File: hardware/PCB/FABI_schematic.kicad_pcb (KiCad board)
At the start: 2 copper layers, 78 x 55 mm, 27 parts, among them J1 Cliff_68125, J10 Conn_01x03_Male, J2 Cliff_68125, J3 Cliff_68125, J4 Cliff_68125, J5 Cliff_68125, J6 Cliff_68125, J7 Cliff_68125, J8 Cliff_68125, J9 Conn_02x05_Odd_Even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

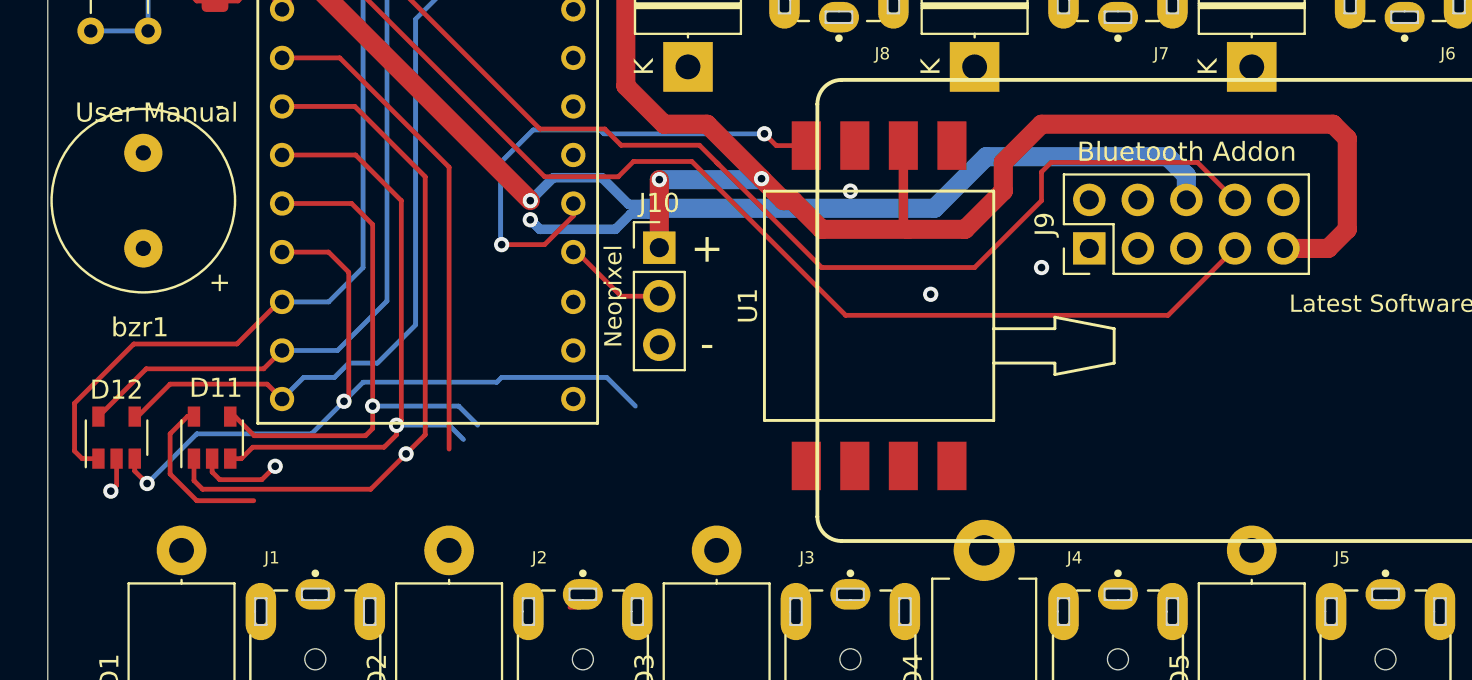
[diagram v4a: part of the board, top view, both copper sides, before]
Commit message: +Display header & 3D design of display to find position Signed-off-by: fussthalerandreas <fussthaler.andreas1997@gmail.com>
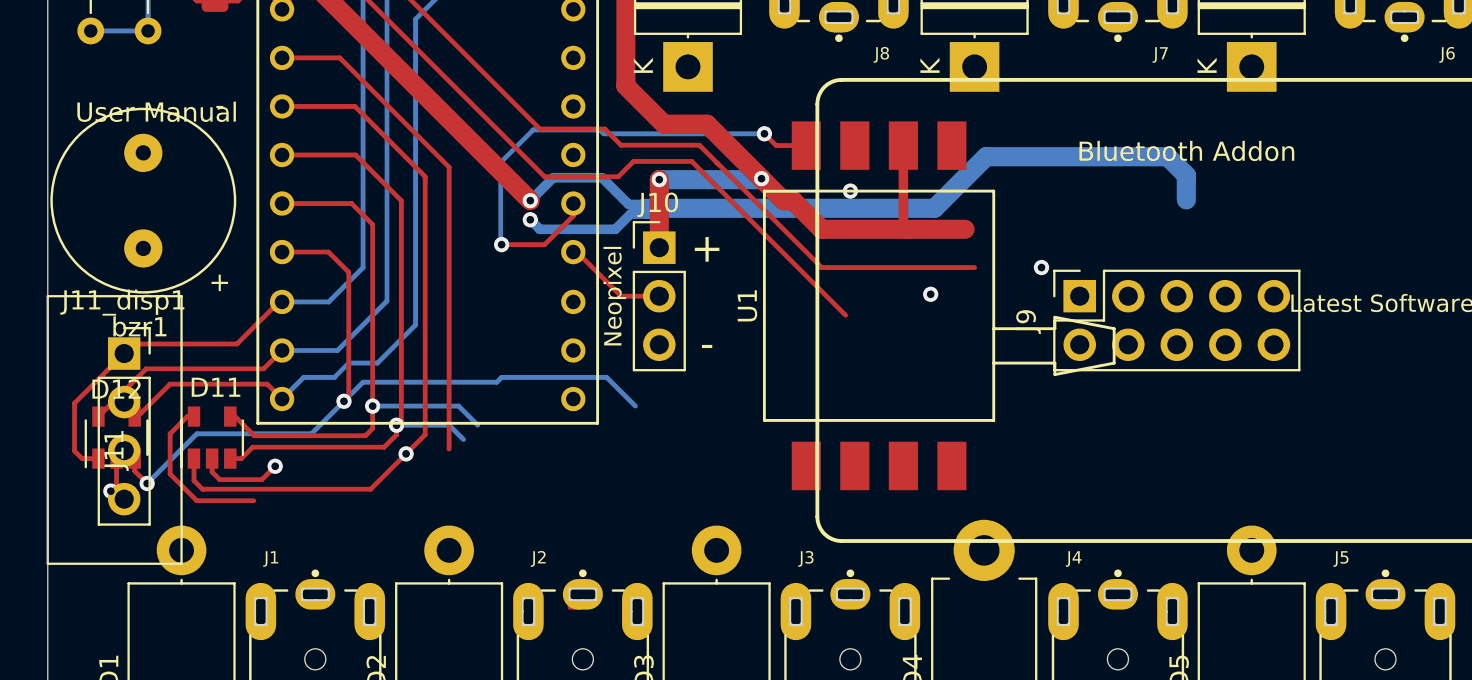
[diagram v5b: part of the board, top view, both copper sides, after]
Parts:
- added J11: Conn_01x04_Male, Connector:display, F.Cu at (76.0, 129.0)
- added J11_disp1: Conn_01x04_Female, Connector_PinSocket_2.54mm:PinSocket_1x04_P2.54mm_Vertical, F.Cu at (77.0, 124.0)
- J9: footprint Connector_PinHeader_2.54mm:PinHeader_2x05_P2.54mm_Vertical -> Connector_PinSocket_2.54mm:PinSocket_2x05_P2.54mm_Vertical
- moved J9 2.55 mm to (127.0, 121.0)
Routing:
- net VCC: track 80.1 -> 48.1 mm
- net /A_RX: track 60.8 -> 38.9 mm
- net /ESP_RX: track 87.6 -> 70.0 mm

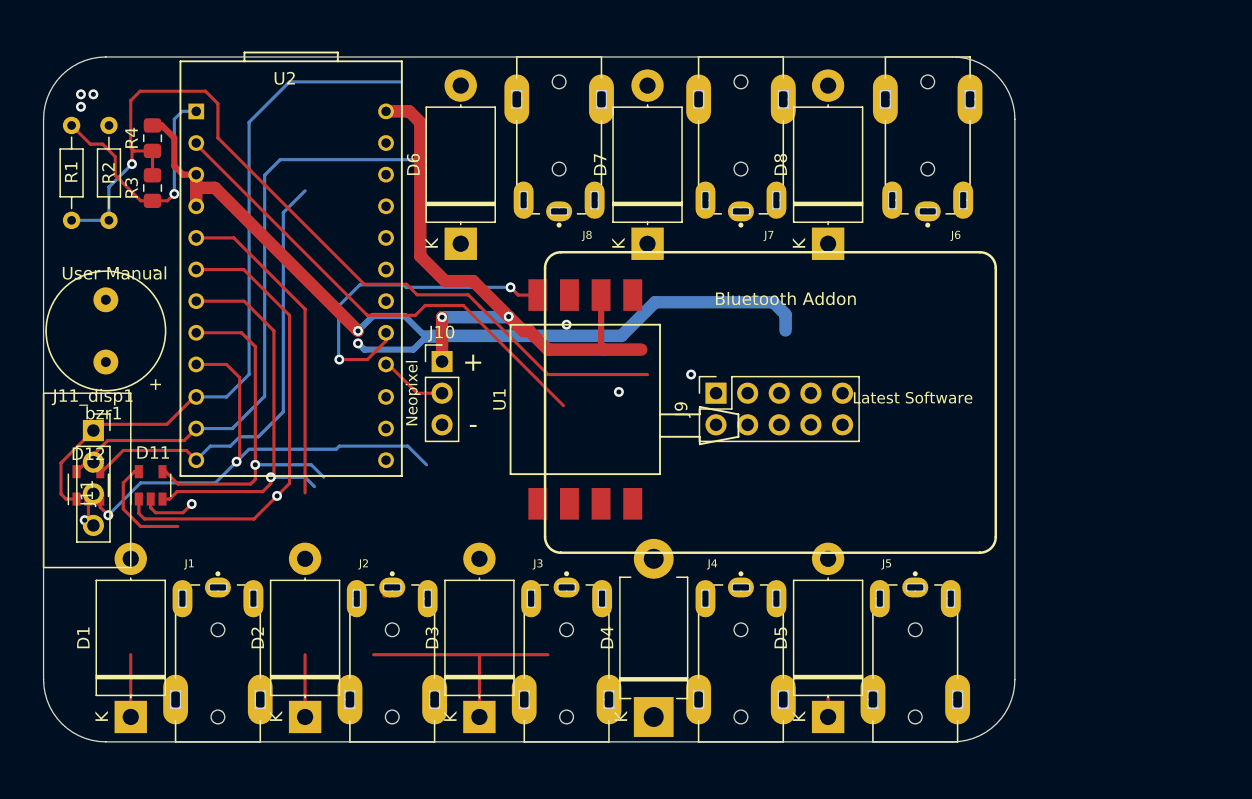
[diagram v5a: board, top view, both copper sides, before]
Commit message: v2 of the PCB: added: Diplay connector, buzzer replaced: JackPlugs repositioned: JackPlugs, TVS, NeoPixel connector, pressure sensor
Signed-off-by: fussthalerandreas <fussthaler.andreas1997@gmail.com>
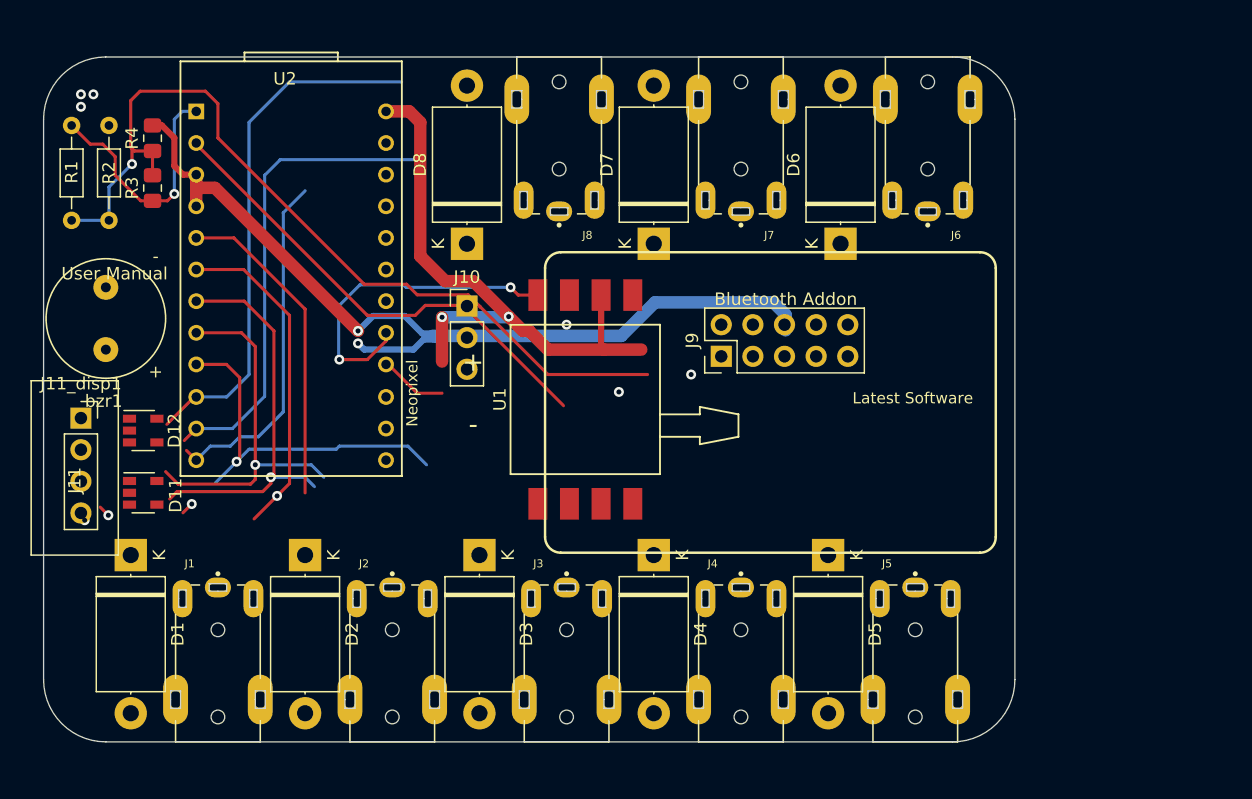
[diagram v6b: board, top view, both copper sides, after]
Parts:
- D4: footprint Diode_THT:D_DO-201AD_P12.70mm_Horizontal -> Diode_THT:D_DO-201AE_P12.70mm_Horizontal
- J9: footprint Connector_PinSocket_2.54mm:PinSocket_2x05_P2.54mm_Vertical -> Connector_PinHeader_2.54mm:PinHeader_2x05_P2.54mm_Vertical
- moved D6 30.5 mm to (137.0, 109.0)
- moved D8 29.0 mm to (107.0, 109.0)
- moved D1 13.0 mm to (80.0, 134.0), turned to 270 degrees
- moved D2 13.0 mm to (94.0, 134.0), turned to 270 degrees
- moved D3 13.0 mm to (108.0, 134.0), turned to 270 degrees
- moved D4 13.0 mm to (122.0, 134.0), turned to 270 degrees
- moved D5 13.0 mm to (136.0, 134.0), turned to 270 degrees
- moved D12 6.22 mm to (81.0, 124.0), turned to 0 degrees
- moved J10 4.89 mm to (107.0, 114.0)
- moved J9 2.99 mm to (127.4, 118.0)
- moved J11 1.41 mm to (75.0, 128.0)
- moved J11_disp1 1.41 mm to (76.0, 123.0)
- moved bzr1 1.00 mm to (78.0, 115.0)
- moved D11 0.85 mm to (81.0, 129.0), turned to 0 degrees
- moved D7 0.50 mm to (122.0, 109.0)
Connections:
- J1 pad 1S: (no net) -> GND
- J1 pad 6SR: GND -> (no net)
- J2 pad 1S: (no net) -> GND
- J2 pad 6SR: GND -> (no net)
- J3 pad 1S: (no net) -> GND
- J3 pad 6SR: GND -> (no net)
- J4 pad 1S: (no net) -> GND
- J4 pad 6SR: GND -> (no net)
- J5 pad 1S: (no net) -> GND
- J5 pad 6SR: GND -> (no net)
- J6 pad 1S: (no net) -> GND
- J6 pad 6SR: GND -> (no net)
- J7 pad 1S: (no net) -> GND
- J7 pad 6SR: GND -> (no net)
- J8 pad 1S: (no net) -> GND
- J8 pad 6SR: GND -> (no net)
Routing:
- net GND: track 109.2 -> 73.8 mm
- net 6: track 55.8 -> 42.1 mm
- net 2: track 37.1 -> 26.5 mm
- net 5: track 40.8 -> 30.5 mm
- net 7: track 48.6 -> 38.9 mm
- net 1: track 34.5 -> 25.9 mm
- net 8: track 35.8 -> 28.2 mm
- net 3: track 32.6 -> 32.0 mm
- net (no net): track 0.52 -> 0.00 mm

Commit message: SMD types of components added, TVS diode orientation, PullUps I2C Signed-off-by: fussthalerandreas <fussthaler.andreas1997@gmail.com>
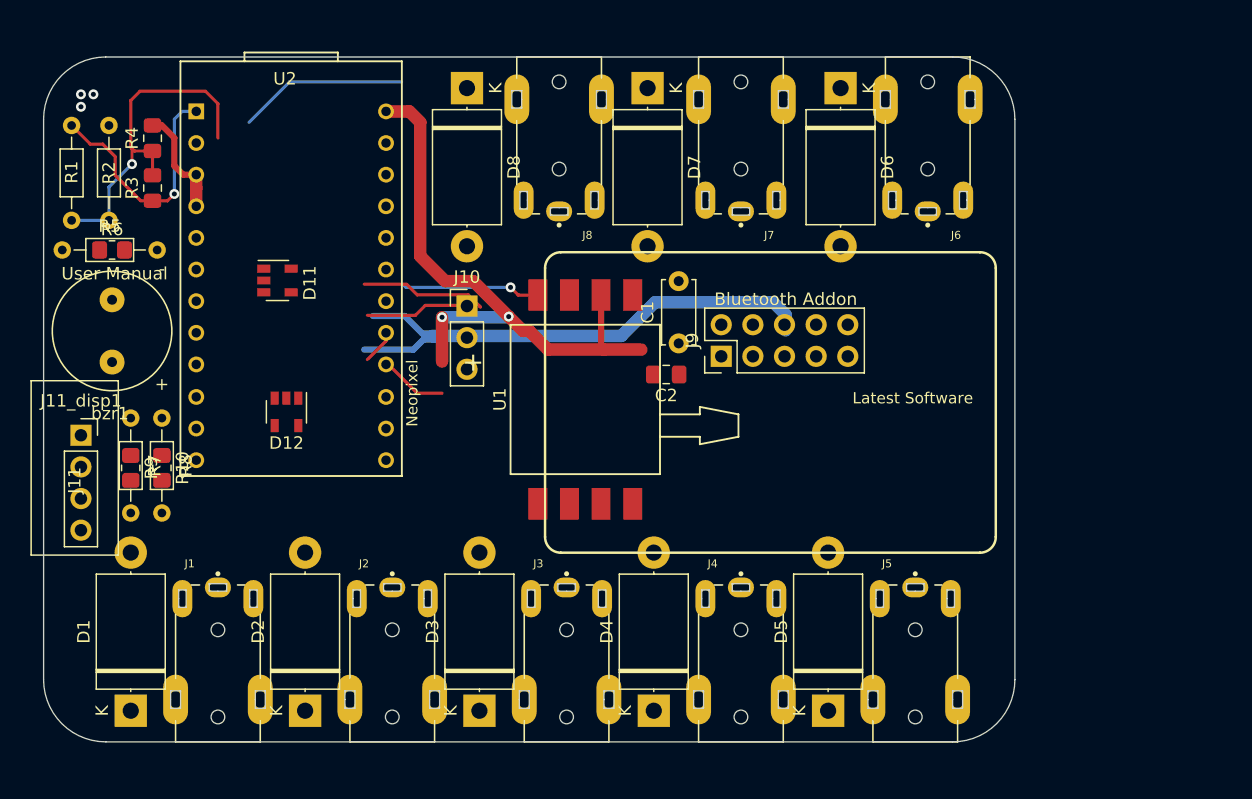
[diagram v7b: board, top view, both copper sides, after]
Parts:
- added C1: 100n, Capacitor_THT:C_Disc_D5.0mm_W2.5mm_P5.00mm, F.Cu at (124.0, 117.0)
- added C2: 100n, Capacitor_SMD:C_0805_2012Metric_Pad1.18x1.45mm_HandSolder, F.Cu at (123.0, 119.5)
- added R10: 4.7k, Resistor_SMD:R_0805_2012Metric_Pad1.20x1.40mm_HandSolder, F.Cu at (82.5, 127.0)
- added R5: 4.7k, Resistor_THT:R_Axial_DIN0204_L3.6mm_D1.6mm_P7.62mm_Horizontal, F.Cu at (74.5, 109.5)
- added R6: 4.7k, Resistor_SMD:R_0805_2012Metric_Pad1.20x1.40mm_HandSolder, F.Cu at (78.5, 109.5)
- added R7: 4.7k, Resistor_THT:R_Axial_DIN0204_L3.6mm_D1.6mm_P7.62mm_Horizontal, F.Cu at (80.0, 123.0)
- added R8: 4.7k, Resistor_THT:R_Axial_DIN0204_L3.6mm_D1.6mm_P7.62mm_Horizontal, F.Cu at (82.5, 123.0)
- added R9: 4.7k, Resistor_SMD:R_0805_2012Metric_Pad1.20x1.40mm_HandSolder, F.Cu at (80.0, 127.0)
- moved D11 20.2 mm to (91.8, 112.0)
- moved D7 12.5 mm to (121.5, 96.5), turned to 270 degrees
- moved D1 12.5 mm to (80.0, 146.5), turned to 90 degrees
- moved D2 12.5 mm to (94.0, 146.5), turned to 90 degrees
- moved D3 12.5 mm to (108.0, 146.5), turned to 90 degrees
- moved D4 12.5 mm to (122.0, 146.5), turned to 90 degrees
- moved D5 12.5 mm to (136.0, 146.5), turned to 90 degrees
- moved D6 12.5 mm to (137.0, 96.5), turned to 270 degrees
- moved D8 12.5 mm to (107.0, 96.5), turned to 270 degrees
- moved D12 11.6 mm to (92.5, 122.5), turned to 270 degrees
- moved J11_disp1 1.38 mm to (76.0, 124.4)
- moved bzr1 1.12 mm to (78.5, 116.0)
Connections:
- D1 pad 1: GND -> 1
- D1 pad 2: 1 -> GND
- D2 pad 1: GND -> 2
- D2 pad 2: 2 -> GND
- D3 pad 1: GND -> 3
- D3 pad 2: 3 -> GND
- D4 pad 1: GND -> 4
- D4 pad 2: 4 -> GND
- D5 pad 1: GND -> 5
- D5 pad 2: 5 -> GND
- D6 pad 1: GND -> 6
- D6 pad 2: 6 -> GND
- D7 pad 1: GND -> 7
- D7 pad 2: 7 -> GND
- D8 pad 1: GND -> 8
- D8 pad 2: 8 -> GND
- bzr1 pad N: GND -> Net-(R5-Pad2)
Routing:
- net 7: track 38.9 -> 0.00 mm
- net /A_RX: track 38.9 -> 0.10 mm
- net /ESP_RX: track 70.0 -> 37.8 mm
- net 3: track 32.0 -> 0.00 mm, vias 1 -> 0
- net 5: track 30.5 -> 0.00 mm, vias 2 -> 0
- net 4: track 29.6 -> 0.00 mm, vias 1 -> 0
- net 6: track 42.1 -> 13.8 mm
- net 8: track 28.2 -> 0.00 mm
- net 2: track 26.5 -> 0.00 mm, vias 1 -> 0
- net 1: track 25.9 -> 0.00 mm
- net GND: track 73.8 -> 52.2 mm, vias 10 -> 3
- net /MPX: track 26.4 -> 13.9 mm, vias 2 -> 1
- net VCC: track 48.1 -> 56.2 mm
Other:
- board text removed: "-"

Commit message: JackPlug Footprint changed
Signed-off-by: fussthalerandreas <fussthaler.andreas1997@gmail.com>
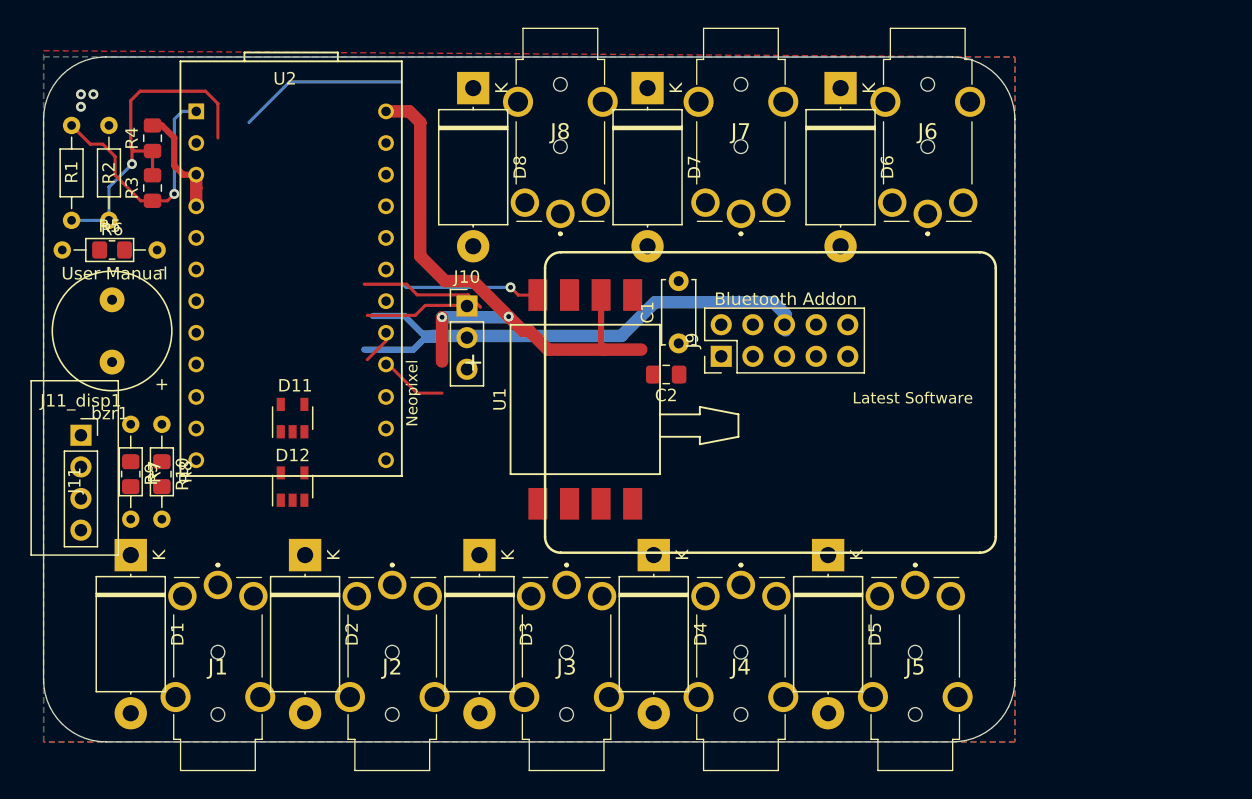
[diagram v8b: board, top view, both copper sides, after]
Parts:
- J1, J2, J3, J4, J5, J6, J7, J8: footprint CLIFF_FC68125:CLIFF_FC68125 -> SamacSys_Parts:FC68125
- moved D1 12.5 mm to (80.0, 134.0), turned to 270 degrees
- moved D2 12.5 mm to (94.0, 134.0), turned to 270 degrees
- moved D3 12.5 mm to (108.0, 134.0), turned to 270 degrees
- moved D4 12.5 mm to (122.0, 134.0), turned to 270 degrees
- moved D5 12.5 mm to (136.0, 134.0), turned to 270 degrees
- moved D11 11.1 mm to (93.0, 123.0), turned to 90 degrees
- moved D12 6.02 mm to (93.0, 128.5), turned to 90 degrees
- moved J8 3.00 mm to (114.5, 100.0), turned to 0 degrees
- moved J1 3.00 mm to (87.0, 143.0), turned to 180 degrees
- moved J2 3.00 mm to (101.0, 143.0), turned to 180 degrees
- moved J3 3.00 mm to (115.0, 143.0), turned to 180 degrees
- moved J4 3.00 mm to (129.0, 143.0), turned to 180 degrees
- moved J5 3.00 mm to (143.0, 143.0), turned to 180 degrees
- moved J6 3.00 mm to (144.0, 100.0), turned to 0 degrees
- moved J7 3.00 mm to (129.0, 100.0), turned to 0 degrees
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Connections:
- J11_disp1 pad 1: 2 -> SDA
- J11_disp1 pad 2: 1 -> SCL
- J9 pad 1: (no net) -> AddOn_Pin1
- J9 pad 2: (no net) -> AddOn_Pin2
- J9 pad 3: (no net) -> AddOn_Pin3
- R10 pad 1: 2 -> SDA
- R7 pad 1: 1 -> SCL
- R8 pad 1: 2 -> SDA
- R9 pad 1: 1 -> SCL
- U2 pad 11: 7 -> 1
- U2 pad 12: 8 -> 2
- U2 pad 13: (no net) -> 8
- U2 pad 14: (no net) -> 7
- U2 pad 15: (no net) -> AddOn_Pin3
- U2 pad 19: (no net) -> AddOn_Pin2
- U2 pad 20: (no net) -> AddOn_Pin1
- U2 pad 5: 1 -> SCL
- U2 pad 6: 2 -> SDA
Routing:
- added copper zone on B.Cu, net GND
- added copper zone on F.Cu, net GND
